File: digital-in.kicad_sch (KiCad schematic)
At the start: 7 parts, among them U4 74HC14

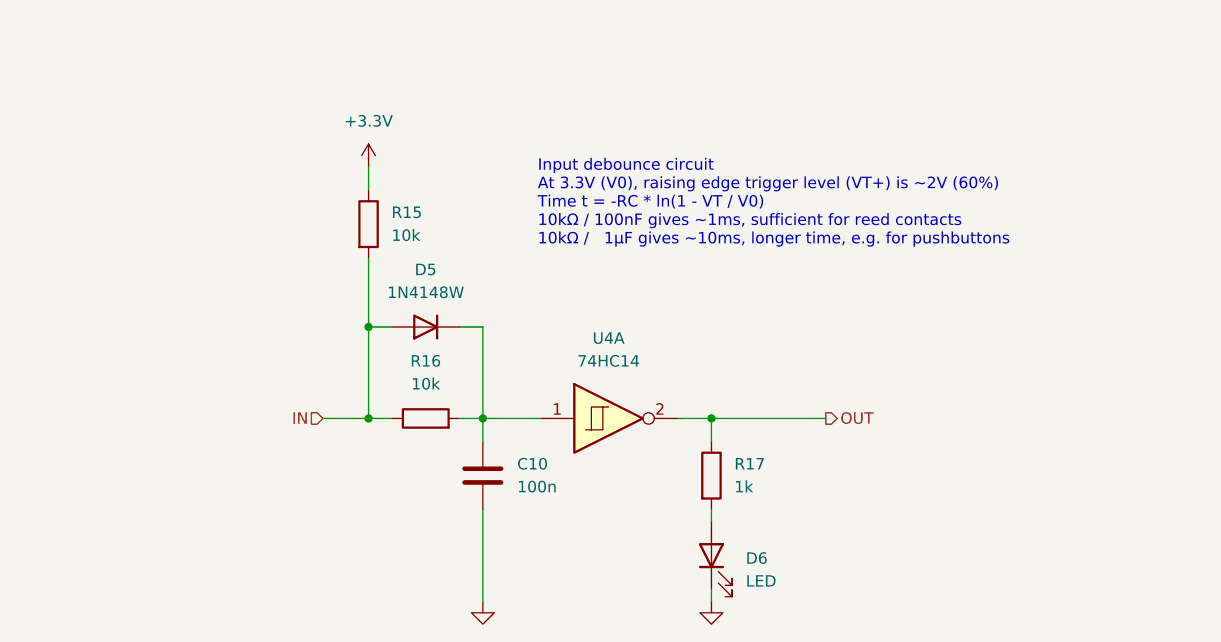
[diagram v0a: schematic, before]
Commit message: Rework digital inputs, add analog inputs and digital outputs
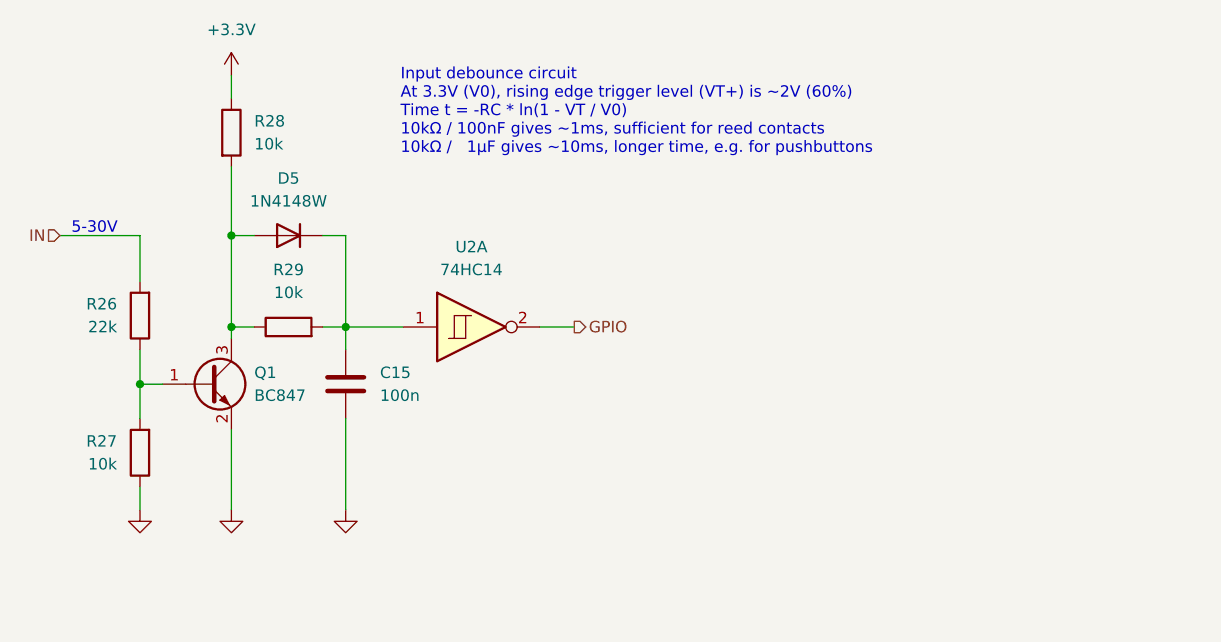
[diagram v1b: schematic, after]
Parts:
- removed D6: LED, LED_THT:LED_D3.0mm, symbol Device:LED
- removed R17: 1k, Resistor_SMD:R_0805_2012Metric, symbol Device:R
- added Q1: BC847, Package_TO_SOT_SMD:SOT-23, symbol Transistor_BJT:BC847
- added R26: 22k, Resistor_SMD:R_0805_2012Metric, symbol Device:R
- added R27: 10k, Resistor_SMD:R_0805_2012Metric, symbol Device:R
- renumbered C10 to C15, R15 to R28, R16 to R29, U4 to U2
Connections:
- net GND: now also Q1.2 (E), R27.1
- net IN: now also R26.2; no longer D5.2 (A), R28.2, R29.1
- net OUT renamed GPIO
- new net: D5.2 (A), Q1.3 (C), R28.2, R29.1
- new net: Q1.1 (B), R26.1, R27.2
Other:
- note added: "5-30V"
- note added: "Input debounce circuit At 3.3V (V0), rising edge trigger level (VT+) is ~2V (60%) Time t = -RC * ln(1 - VT / V0) 10kΩ / 100nF gives ~1ms, sufficient for reed contacts 10kΩ / 1µF gives ~10ms, longer time, e.g. for pushbuttons"
- note removed: "Input debounce circuit At 3.3V (V0), raising edge trigger level (VT+) is ~2V (60%) Time t = -RC * ln(1 - VT / V0) 10kΩ / 100nF gives ~1ms, sufficient for reed contacts 10kΩ / 1µF gives ~10ms, longer time, e.g. for pushbuttons"
- moved on the sheet: C15, D5, R28, R29, U2A
